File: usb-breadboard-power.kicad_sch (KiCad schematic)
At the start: 39 parts, among them J1 USB_C_Receptacle_PowerOnly_6P, J2 Conn_02x02_Counter_Clockwise, J3 Conn_02x02_Counter_Clockwise, Q3 Q_Dual_NMOS, SW1 SW_DIP_x03, U2 BD33FC0FP, U3 LM339

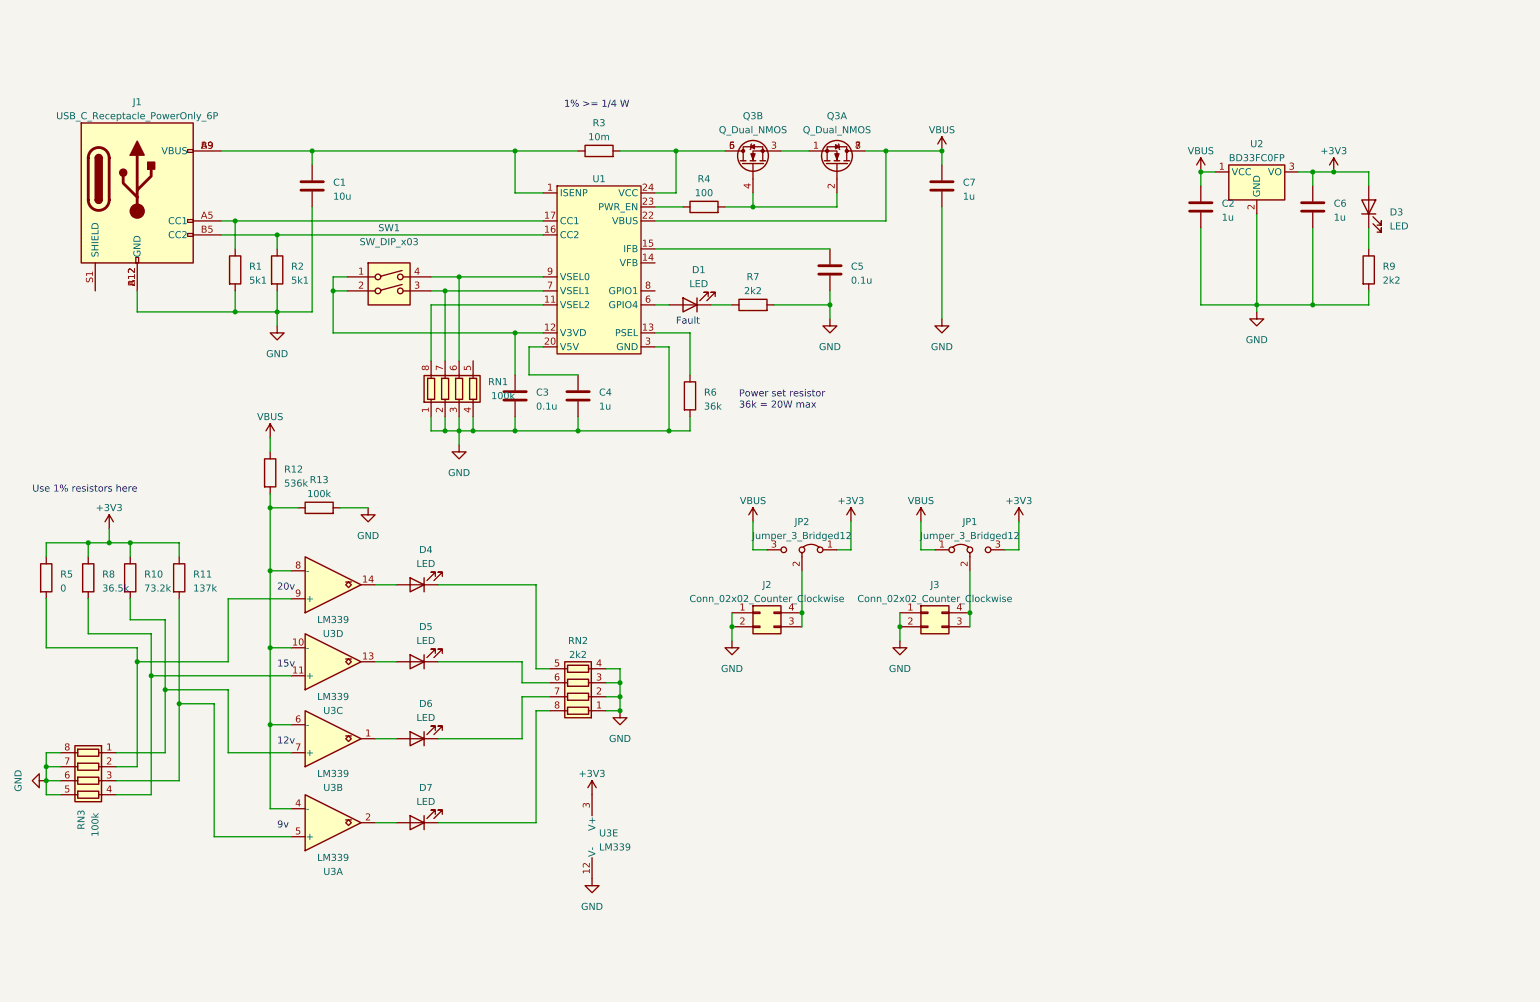
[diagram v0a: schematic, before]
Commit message: Swapped IC to one that supports 12v
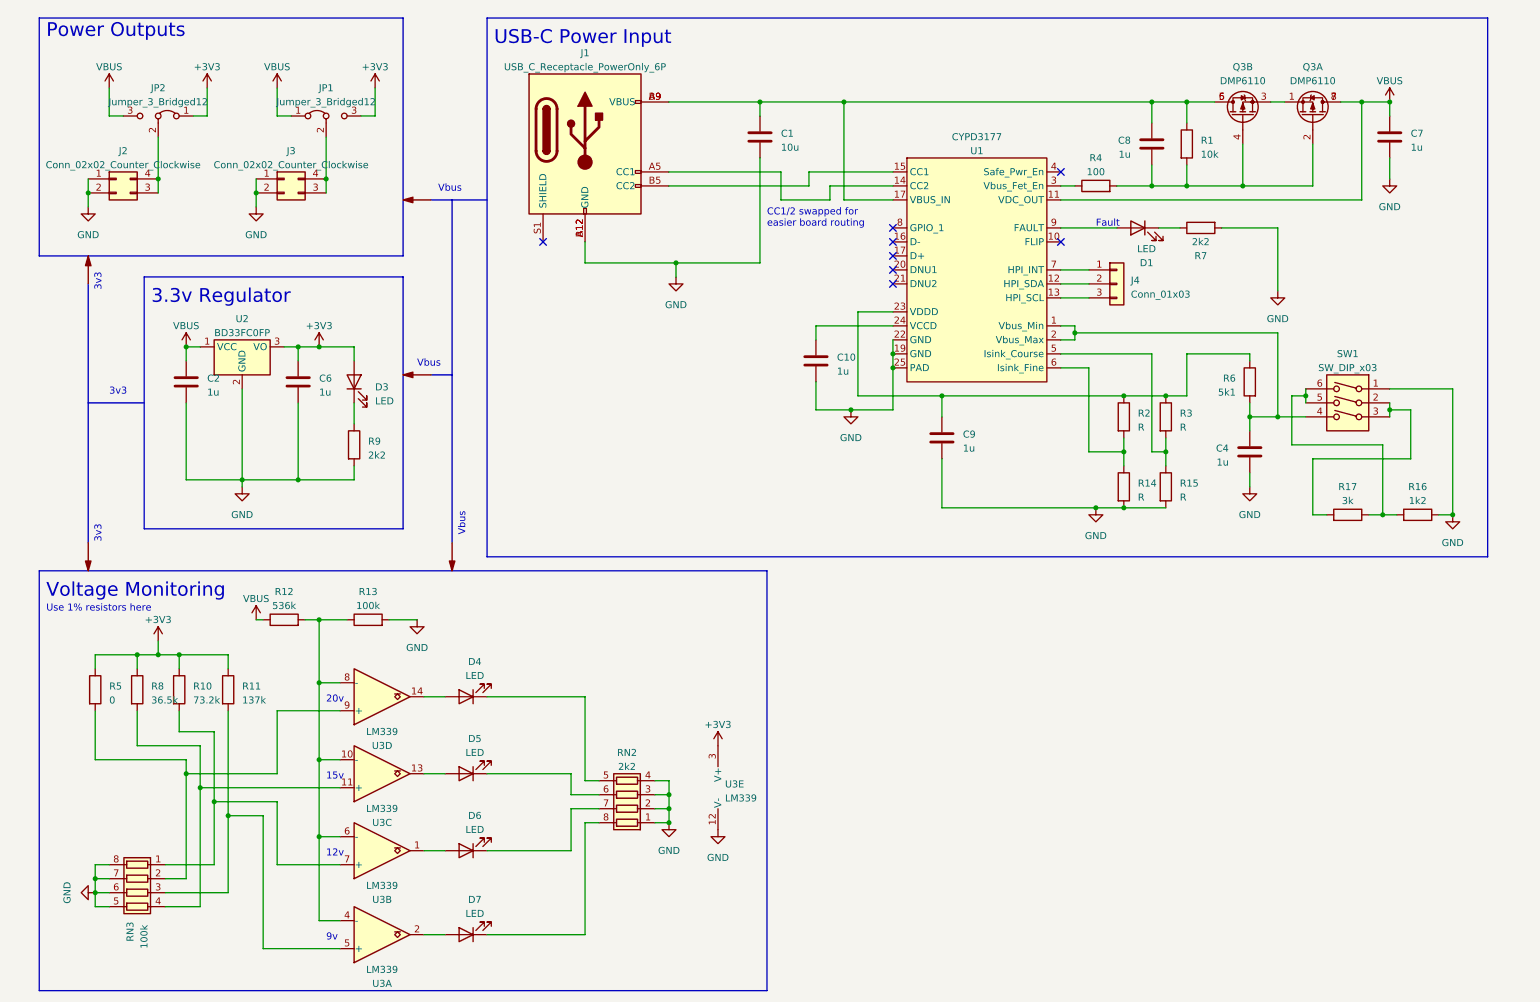
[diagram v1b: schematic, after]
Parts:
- removed C3, C5: 0.1u, Capacitor_SMD:C_1206_3216Metric, symbol Device:C
- removed Q3: Q_Dual_NMOS, Package_SO:SOIC-8_3.9x4.9mm_P1.27mm, symbol Device:Q_Dual_NMOS_G1S2G2D2S1D1
- removed RN1: 100k, Resistor_SMD:R_Array_Convex_4x1206, symbol Device:R_Pack04
- removed SW1: SW_DIP_x03, Button_Switch_SMD:SW_DIP_SPSTx02_Slide_6.7x6.64mm_W8.61mm_P2.54mm_LowProfile, symbol Switch:SW_DIP_x02
- removed U1: ~, Package_DFN_QFN:WQFN-24-1EP_4x4mm_P0.5mm_EP2.6x2.6mm, symbol usb-breadboard:AP33771
- added C10, C8, C9: 1u, Capacitor_SMD:C_1206_3216Metric, symbol Device:C
- added J4: Conn_01x03, Connector_PinHeader_2.54mm:PinHeader_1x03_P2.54mm_Vertical_SMD_Pin1Left, symbol Connector_Generic:Conn_01x03
- added Q3: DMP6110, Package_SO:SO-8_5.3x6.2mm_P1.27mm, symbol Device:Q_Dual_PMOS_S1G1D2S2G2D1
- added R14, R15: R, Resistor_SMD:R_1206_3216Metric, symbol Device:R
- added R16: 1k2, Resistor_SMD:R_1206_3216Metric, symbol Device:R
- added R17: 3k, Resistor_SMD:R_1206_3216Metric, symbol Device:R
- added SW1: SW_DIP_x03, Button_Switch_SMD:SW_DIP_SPSTx03_Slide_6.7x9.18mm_W8.61mm_P2.54mm_LowProfile, symbol Switch:SW_DIP_x03
- added U1: CYPD3177, Package_DFN_QFN:QFN-24-1EP_4x4mm_P0.5mm_EP2.8x2.8mm, symbol usb-breadboard:CYPD3177
- R1: value 5k1 -> 10k; DPN RMCF1206JT5K10CT-ND -> (none); MPN RMCF1206JT5K10 -> (none)
- R2: value 5k1 -> R; DPN RMCF1206JT5K10CT-ND -> (none); MPN RMCF1206JT5K10 -> (none)
- R3: value 10m -> R; DPN 13-PA1206FRE070R01ZCT-ND -> (none); MPN PA1206FRE070R01Z -> (none)
- R6: value 36k -> 5k1; DPN 738-RMCF0402FT36K0CT-ND -> (none); MPN RMCF0402FT36K0 -> (none)
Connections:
- net GND: now also C10.2, C9.2, R14.2, R15.2, R16.1, SW1.1, U1.19 (GND), U1.22 (GND), U1.25 (PAD); no longer R1.2, R2.2, R6.2
- net VBUS: now also Q3.7 (D), Q3.8 (D), U1.11 (VDC_OUT)
- net at C4.1: now also R6.2, SW1.4, U1.1 (Vbus_Min), U1.2 (Vbus_Max)
- net at R6.1: now also R2.1, R3.1, C9.1, U1.23 (VDDD)
- net at D1.2 (A): now also U1.9 (FAULT)
- net at R4.2: now also R1.2, C8.2, Q3.2 (G), Q3.4 (G)
- net at R3.2: now also R15.1, U1.5 (Isink_Course)
- net at C1.1, J1.A9 (VBUS), J1.B9 (VBUS): now also R1.1, C8.1, Q3.5 (D), Q3.6 (D), U1.17 (VBUS_IN); no longer R3.1
- net at J1.B5 (CC2): now also U1.15 (CC1); no longer R2.1
- net at J1.A5 (CC1): now also U1.14 (CC2); no longer R1.1
- net at R4.1: now also U1.3 (Vbus_Fet_En)
- new net: J4.1 (Pin_1), U1.7 (HPI_INT)
- new net: J4.2 (Pin_2), U1.12 (HPI_SDA)
- new net: J4.3 (Pin_3), U1.13 (HPI_SCL)
- new net: R16.2, R17.1, SW1.5, SW1.6
- new net: C10.1, U1.24 (VCCD)
- new net: R14.1, R2.2, U1.6 (Isink_Fine)
- new net: R17.2, SW1.2, SW1.3
- new net: Q3.1 (S), Q3.3 (S)
- no-connect marks 0 -> 8
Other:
- note added: "3.3v Regulator"
- note added: "3v3"
- note added: "CC1/2 swapped for easier board routing"
- note added: "Power Outputs"
- note added: "USB-C Power Input"
- note added: "Vbus"
- note added: "Voltage Monitoring"
- note removed: "1% >= 1/4 W"
- note removed: "Power set resistor 36k = 20W max"
- moved on the sheet: C1, C2, C4, C6, C7, D1, D3, D4, D5, D6, D7, J1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

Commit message: Cleaned up schematic and added Vbus LED
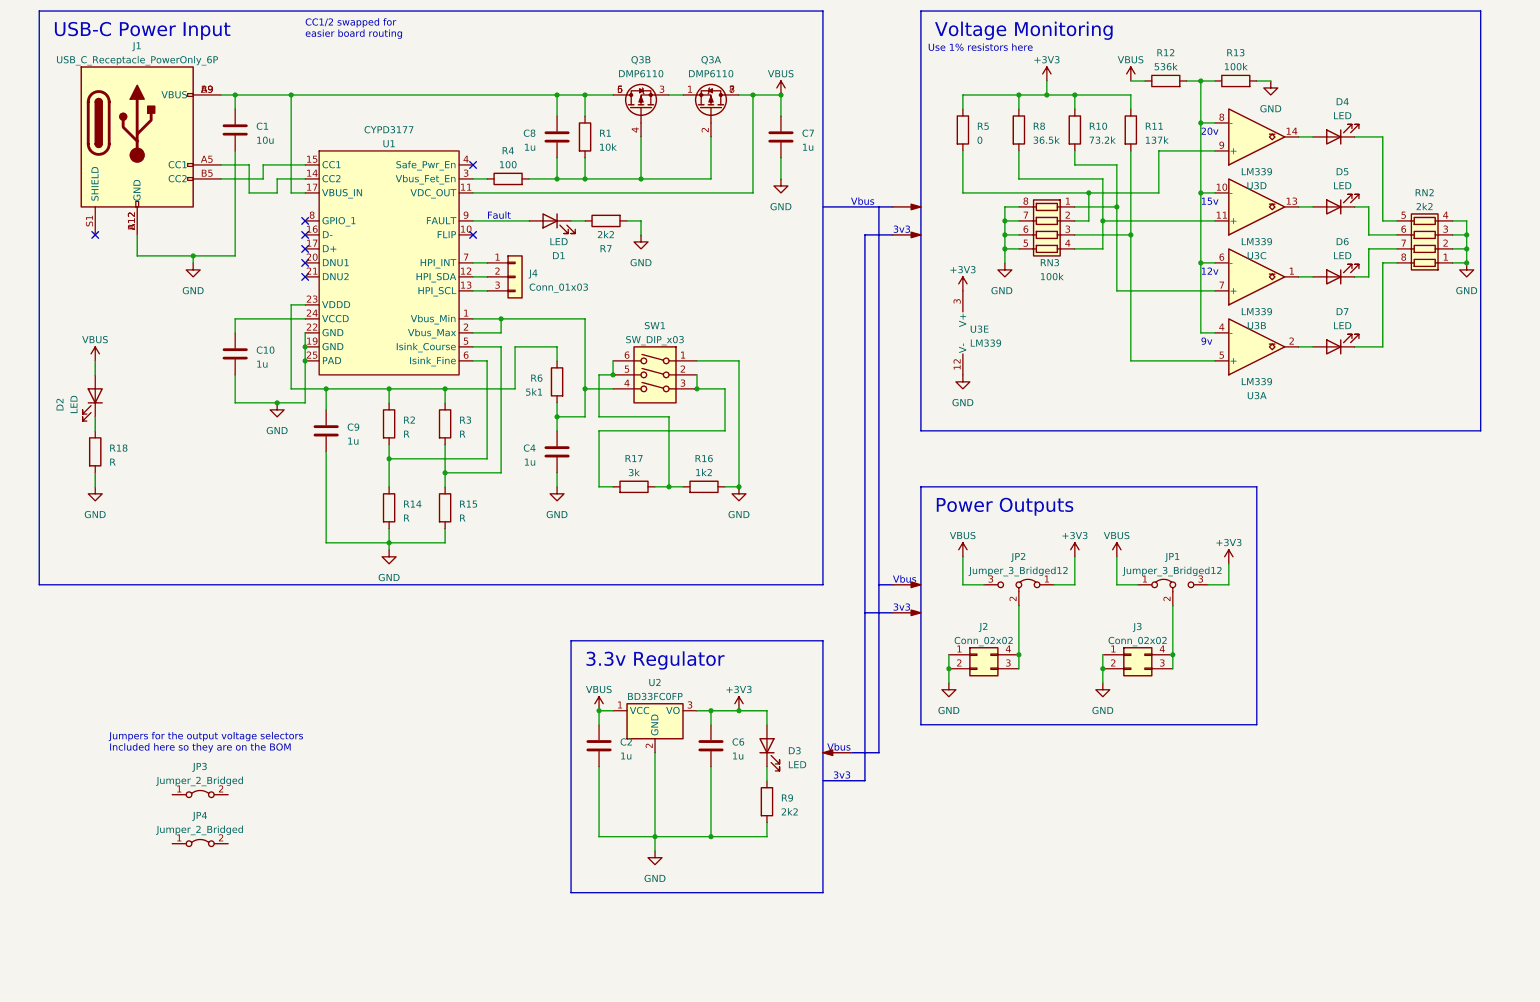
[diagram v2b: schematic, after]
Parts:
- added D2: LED, LED_SMD:LED_1206_3216Metric, symbol Device:LED
- added JP3, JP4: Jumper_2_Bridged, symbol Jumper:Jumper_2_Bridged
- added R18: R, Resistor_SMD:R_1206_3216Metric, symbol Device:R
- J2, J3: value Conn_02x02_Counter_Clockwise -> Conn_02x02
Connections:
- net GND: now also R18.2
- net VBUS: now also D2.2 (A)
- net at U1.17 (VBUS_IN): now also C1.1, C8.1, J1.A9 (VBUS), J1.B9 (VBUS), Q3.5 (D), Q3.6 (D), R1.1
- new net: D2.1 (K), R18.1
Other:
- note added: "Jumpers for the output voltage selectors Included here so they are on the BOM"
- company: (none) -> Benjamin Crall
- title: (none) -> USB-C Breadboard Power Supply
- moved on the sheet: C1, C10, C2, C4, C6, C7, C8, C9, D1, D3, D4, D5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

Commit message: Updated Mouser BOM
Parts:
- C1: DPN-m (none) -> 187-CL31A106KAHNNNE; MPN-m (none) -> CL31A106KAHNNNE
- C10, C2, C4, C6, C7, C8, C9: DPN-m (none) -> 187-CL31B105KAHNNNE; MPN-m (none) -> CL31B105KAHNNNE
- D1, D2, D3, D4, D5, D6, D7: DPN-m (none) -> 645-599-0411-127F; MPN-m (none) -> 599-0411-127F
- J1: footprint usb-breadboard:usbc -> usb-breadboard:J-Amphenol-USB-C; DPN-m (none) -> 649-10164359-00011LF; MPN-m (none) -> 10164359-00011LF
- J2, J3: DPN-m (none) -> 649-1012938190403BLF; MPN-m (none) -> 10129381-904003BLF
- J4, JP1, JP2: DPN-m (none) -> 649-1012938090301ALF; MPN-m (none) -> 10129380-903001ALF
- Q3: MPN-m (none) -> DMP6110SSDQ-13; price 0.605 -> (none)
- R1: DPN-m (none) -> 652-CR1206FX-1002ELF; MPN-m (none) -> CR1206-FX-1002ELF
- R10: DPN-m (none) -> 652-CR1206FX-7322ELF; MPN-m (none) -> CR1206-FX-7322ELF
- R11: DPN-m (none) -> 652-CR1206FX-1373ELF; MPN-m (none) -> CR1206-FX-1373ELF
- R12: DPN-m (none) -> 652-CR1206FX-5363ELF; MPN-m (none) -> CR1206-FX-5363ELF
- R13: DPN-m (none) -> 652-CR1206FX-1003ELF; MPN-m (none) -> CR1206-FX-1003ELF
- R14: value R -> 0; DPN-m (none) -> 652-CR1206-J/-000ELF; MPN-m (none) -> CR1206-J/-000ELF
- R15: value R -> 2k2; DPN-m (none) -> 652-CR1206FX-2201ELF; MPN-m (none) -> CR1206-FX-2201ELF
- R16: DPN-m (none) -> 652-CR1206FX-1201ELF; MPN-m (none) -> CR1206-FX-1201ELF
- R17: DPN-m (none) -> 652-CR1206FX-3001ELF; MPN-m (none) -> CR1206-FX-3001ELF
- R18, R3: value R -> 5k1; DPN-m (none) -> 652-CR1206FX-5101ELF; MPN-m (none) -> CR1206FX-5101ELF
- R2: value R -> DNP
- R4: DPN-m (none) -> 652-CR1206FX-1000ELF; MPN-m (none) -> CR1206-FX-1000ELF
- R5: DPN-m (none) -> 652-CR1206-J/-000ELF; MPN-m (none) -> CR1206-J/-000ELF
- R6: DPN-m (none) -> 652-CR1206FX-5101ELF; MPN-m (none) -> CR1206FX-5101ELF
- R7, R9: DPN-m (none) -> 652-CR1206FX-2201ELF; MPN-m (none) -> CR1206-FX-2201ELF
- R8: DPN-m (none) -> 652-CR1206FX-3652ELF; MPN-m (none) -> CR1206-FX-3652ELF
- RN2: DPN-m (none) -> 603-YC164-FR-072K2L; MPN-m (none) -> YC164-FR-072K2L
- RN3: DPN-m (none) -> 603-TC164-FR-07100KL; MPN-m (none) -> TC164-FR-07100KL
- SW1: MPN-m (none) -> DS04-254-2-03BK-SMT; price 0.582 -> (none)
- U1: MPN-m (none) -> CYPD3177-24LQXQT; price 2.25 -> (none)
- U2: DPN-m (none) -> 621-AZ1084CD-3.3TRG1; MPN-m (none) -> CYPD3177-24LQXQT
- U3: DPN-m (none) -> 595-LM339AN; MPN-m (none) -> LM339AN
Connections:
- net at U1.17 (VBUS_IN): now also C1.1, C8.1, J1.A9 (VBUS), J1.B9 (VBUS), Q3.5 (D), Q3.6 (D), R1.1

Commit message: Fixed BOM errors
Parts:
- D1, D2, D3, D4, D5, D6, D7: DPN-m 645-599-0411-127F -> 710-156120RS75000; MPN-m 599-0411-127F -> 156120RS75000
- U3: DPN-m 595-LM339AN -> 595-LM339PWRG4; MPN-m LM339AN -> LM339PWRG4
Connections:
- net at U1.17 (VBUS_IN): now also C1.1, C8.1, J1.A9 (VBUS), J1.B9 (VBUS), Q3.5 (D), Q3.6 (D), R1.1
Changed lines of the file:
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@@
       (effects (font (size 1.27 1.27)) hide)
     )
-    (property "DPN-m" "645-599-0411-127F" (at 27.94 87.63 0)
-      (effects (font (size 1.27 1.27)) hide)
-    )
-    (property "MPN-m" "599-0411-127F " (at 27.94 87.63 0)
+    (property "DPN-m" "710-156120RS75000 " (at 27.94 87.63 0)
+      (effects (font (size 1.27 1.27)) hide)
+    )
+    (property "MPN-m" "156120RS75000 " (at 27.94 87.63 0)
       (effects (font (size 1.27 1.27)) hide)
     )
@@
       (effects (font (size 1.27 1.27)) hide)
     )
-    (property "DPN-m" "595-LM339AN" (at 238.76 40.64 0)
-      (effects (font (size 1.27 1.27)) hide)
-    )
-    (property "MPN-m" "LM339AN " (at 238.76 40.64 0)
+    (property "DPN-m" "595-LM339PWRG4" (at 238.76 40.64 0)
+      (effects (font (size 1.27 1.27)) hide)
+    )
+    (property "MPN-m" "LM339PWRG4 " (at 238.76 40.64 0)
       (effects (font (size 1.27 1.27)) hide)
     )
@@
       (effects (font (size 1.27 1.27)) hide)
     )
-    (property "DPN-m" "595-LM339AN" (at 238.76 78.74 0)
-      (effects (font (size 1.27 1.27)) hide)
-    )
-    (property "MPN-m" "LM339AN " (at 238.76 78.74 0)
+    (property "DPN-m" "595-LM339PWRG4" (at 238.76 78.74 0)
+      (effects (font (size 1.27 1.27)) hide)
+    )
+    (property "MPN-m" "LM339PWRG4 " (at 238.76 78.74 0)
       (effects (font (size 1.27 1.27)) hide)
     )
@@
       (effects (font (size 1.27 1.27)) hide)
     )
-    (property "DPN-m" "595-LM339AN" (at 187.96 76.2 0)
-      (effects (font (size 1.27 1.27)) hide)
-    )
-    (property "MPN-m" "LM339AN " (at 187.96 76.2 0)
+    (property "DPN-m" "595-LM339PWRG4" (at 187.96 76.2 0)
+      (effects (font (size 1.27 1.27)) hide)
+    )
+    (property "MPN-m" "LM339PWRG4 " (at 187.96 76.2 0)
       (effects (font (size 1.27 1.27)) hide)
     )
@@
       (effects (font (size 1.27 1.27)) hide)
     )
-    (property "DPN-m" "645-599-0411-127F" (at 110.49 55.88 0)
-      (effects (font (size 1.27 1.27)) hide)
-    )
-    (property "MPN-m" "599-0411-127F " (at 110.49 55.88 0)
+    (property "DPN-m" "710-156120RS75000 " (at 110.49 55.88 0)
+      (effects (font (size 1.27 1.27)) hide)
+    )
+    (property "MPN-m" "156120RS75000 " (at 110.49 55.88 0)
       (effects (font (size 1.27 1.27)) hide)
     )
@@
       (effects (font (size 1.27 1.27)) hide)
     )
-    (property "DPN-m" "645-599-0411-127F" (at 252.73 53.34 0)
-      (effects (font (size 1.27 1.27)) hide)
-    )
-    (property "MPN-m" "599-0411-127F " (at 252.73 53.34 0)
+    (property "DPN-m" "710-156120RS75000 " (at 252.73 53.34 0)
+      (effects (font (size 1.27 1.27)) hide)
+    )
+    (property "MPN-m" "156120RS75000 " (at 252.73 53.34 0)
       (effects (font (size 1.27 1.27)) hide)
     )
@@
       (effects (font (size 1.27 1.27)) hide)
     )
-    (property "DPN-m" "645-599-0411-127F" (at 149.86 151.13 0)
-      (effects (font (size 1.27 1.27)) hide)
-    )
-    (property "MPN-m" "599-0411-127F " (at 149.86 151.13 0)
+    (property "DPN-m" "710-156120RS75000 " (at 149.86 151.13 0)
+      (effects (font (size 1.27 1.27)) hide)
+    )
+    (property "MPN-m" "156120RS75000 " (at 149.86 151.13 0)
       (effects (font (size 1.27 1.27)) hide)
     )
@@
       (effects (font (size 1.27 1.27)) hide)
     )
-    (property "DPN-m" "595-LM339AN" (at 238.76 53.34 0)
-      (effects (font (size 1.27 1.27)) hide)
-    )
-    (property "MPN-m" "LM339AN " (at 238.76 53.34 0)
+    (property "DPN-m" "595-LM339PWRG4" (at 238.76 53.34 0)
+      (effects (font (size 1.27 1.27)) hide)
+    )
+    (property "MPN-m" "LM339PWRG4 " (at 238.76 53.34 0)
       (effects (font (size 1.27 1.27)) hide)
     )
@@
       (effects (font (size 1.27 1.27)) hide)
     )
-    (property "DPN-m" "645-599-0411-127F" (at 252.73 40.64 0)
-      (effects (font (size 1.27 1.27)) hide)
-    )
-    (property "MPN-m" "599-0411-127F " (at 252.73 40.64 0)
+    (property "DPN-m" "710-156120RS75000 " (at 252.73 40.64 0)
+      (effects (font (size 1.27 1.27)) hide)
+    )
+    (property "MPN-m" "156120RS75000 " (at 252.73 40.64 0)
       (effects (font (size 1.27 1.27)) hide)
     )
@@
       (effects (font (size 1.27 1.27)) hide)
     )
-    (property "DPN-m" "595-LM339AN" (at 238.76 66.04 0)
-      (effects (font (size 1.27 1.27)) hide)
-    )
-    (property "MPN-m" "LM339AN " (at 238.76 66.04 0)
+    (property "DPN-m" "595-LM339PWRG4" (at 238.76 66.04 0)
+      (effects (font (size 1.27 1.27)) hide)
+    )
+    (property "MPN-m" "LM339PWRG4 " (at 238.76 66.04 0)
       (effects (font (size 1.27 1.27)) hide)
     )
@@
       (effects (font (size 1.27 1.27)) hide)
     )
-    (property "DPN-m" "645-599-0411-127F" (at 252.73 66.04 0)
-      (effects (font (size 1.27 1.27)) hide)
-    )
-    (property "MPN-m" "599-0411-127F " (at 252.73 66.04 0)
+    (property "DPN-m" "710-156120RS75000 " (at 252.73 66.04 0)
+      (effects (font (size 1.27 1.27)) hide)
+    )
+    (property "MPN-m" "156120RS75000 " (at 252.73 66.04 0)
       (effects (font (size 1.27 1.27)) hide)
     )
@@
       (effects (font (size 1.27 1.27)) hide)
     )
-    (property "DPN-m" "645-599-0411-127F" (at 252.73 78.74 0)
-      (effects (font (size 1.27 1.27)) hide)
-    )
-    (property "MPN-m" "599-0411-127F " (at 252.73 78.74 0)
-      (effects (font (size 1.27 1.27)) hide)
-    )
+    (property "DPN-m" "710-156120RS75000 " (at 252.73 78.74 0)
+      (effects (font (size 1.27 1.27)) hide)
+    )
+    (property "MPN-m" "156120RS75000 " (at 252.73 78.74 0)
+      (effects (font (size 1.27 1.27)) hide)
+    )
